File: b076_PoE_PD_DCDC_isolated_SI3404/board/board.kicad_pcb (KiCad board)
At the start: 2 copper layers, 45 x 29 mm, 40 parts, among them J1 013_PoE_rectified, J2 003_power, U1 Si3404, U2 FOD817A3SD, U3 TLV431

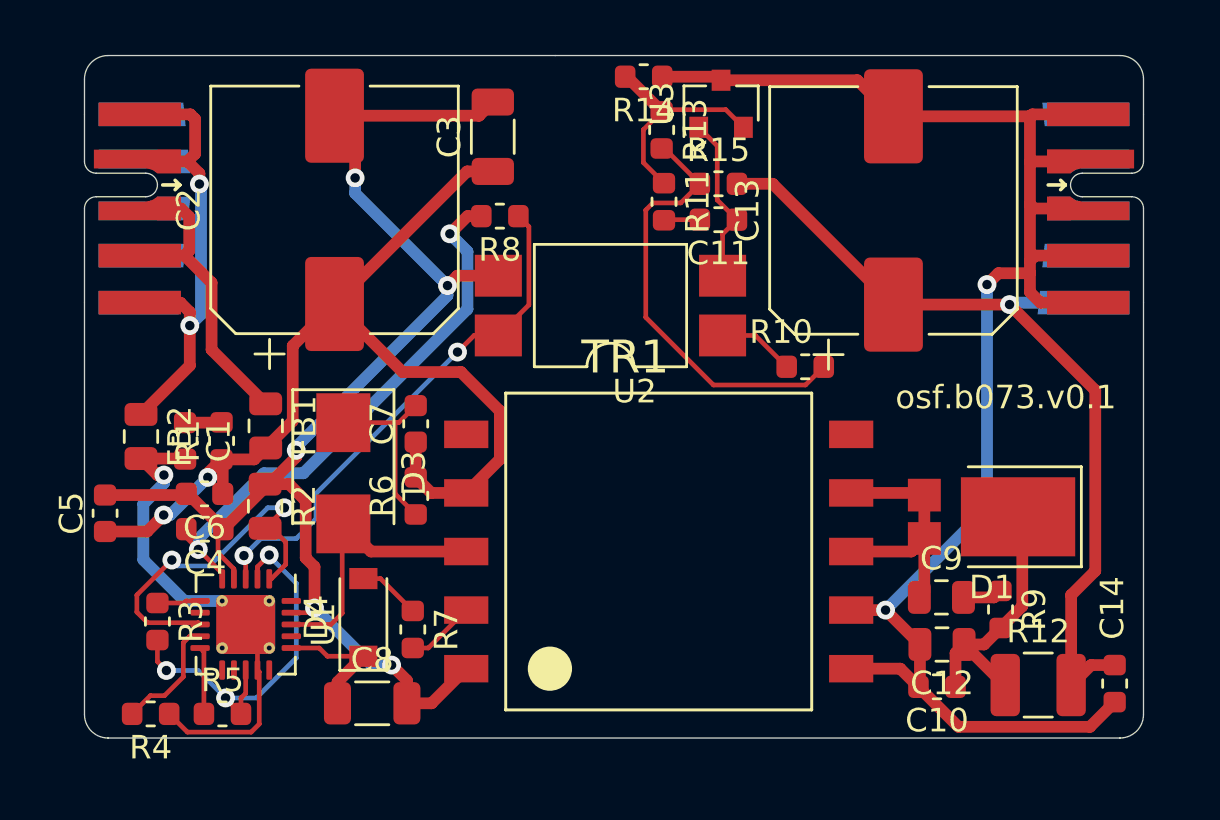
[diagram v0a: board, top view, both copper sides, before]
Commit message: cleaned up silkscreen
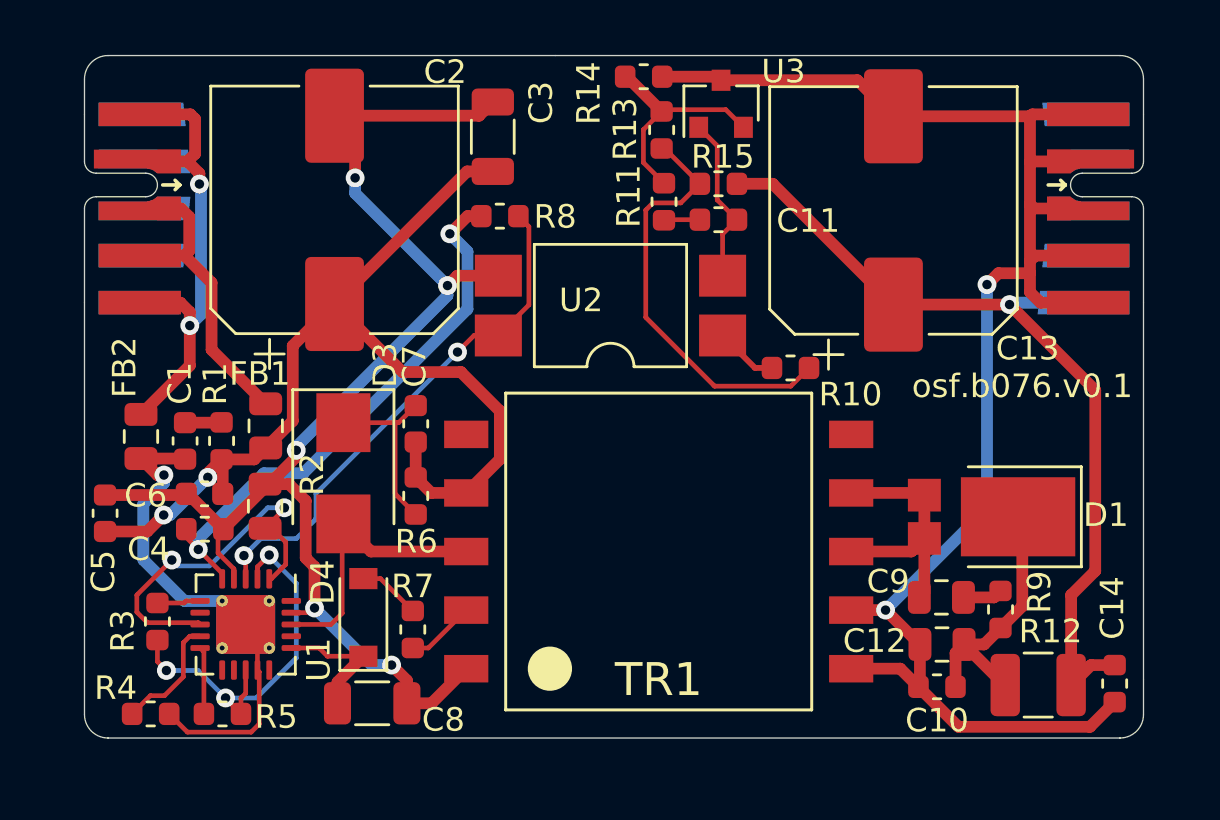
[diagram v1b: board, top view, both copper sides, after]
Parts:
- moved R10 0.63 mm to (160.0, 97.3)
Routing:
- net Net-(R10-Pad2): track 18.6 -> 18.0 mm
- net Net-(R10-Pad1): track 3.27 -> 2.67 mm
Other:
- board text added: "osf.b076.v0.1"
- board text removed: "osf.b073.v0.1"

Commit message: Update Symbol and relayout b076 dcdc
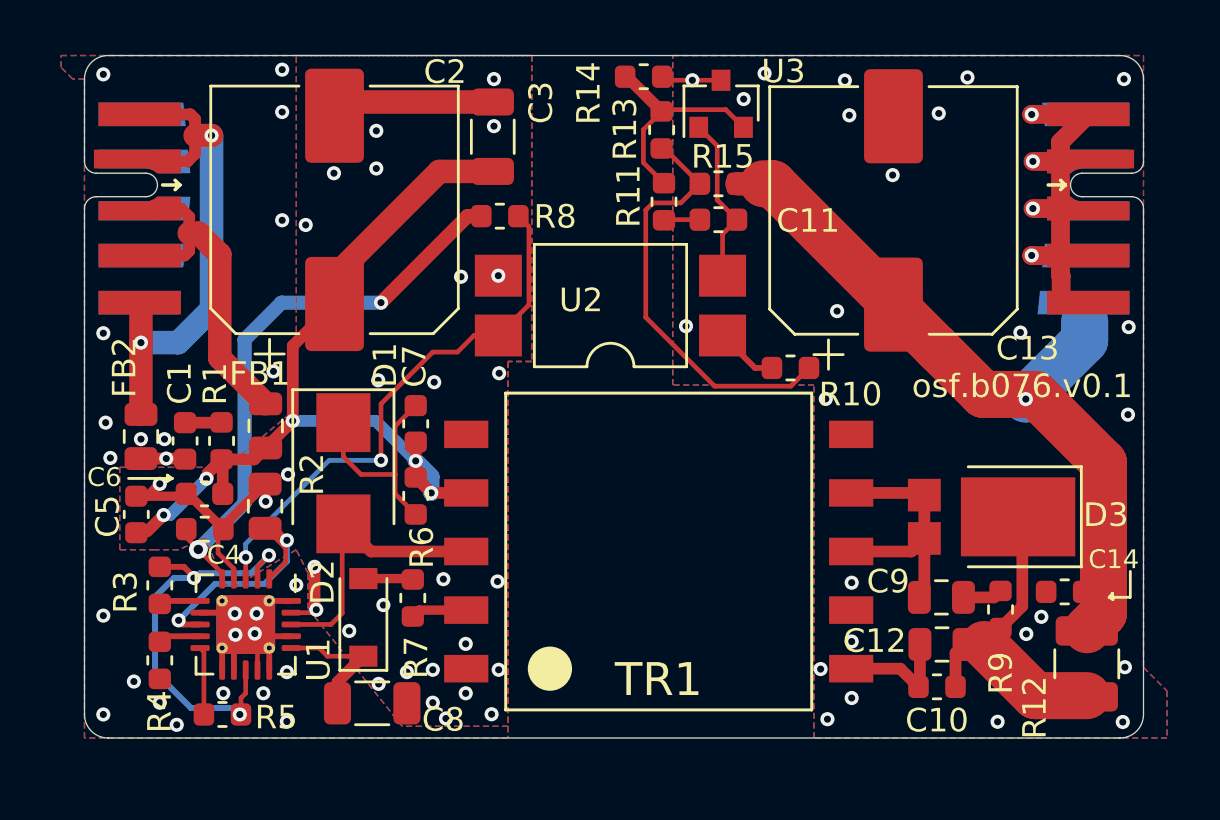
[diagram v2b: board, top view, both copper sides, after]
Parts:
- D3: renamed from D1; value SDT10A45P5 -> SDT10A45P5-13D
- TR1: value 749119950 -> TRANSF6
- U2: value FOD817A3SD -> LTV-827
- moved C14 4.44 mm to (171.7, 106.8), turned to 180 degrees
- moved R4 2.31 mm to (133.2, 109.7), turned to 90 degrees
- moved R12 2.25 mm to (172.6, 109.8), turned to 90 degrees
- moved R3 1.54 mm to (133.2, 106.5), turned to 90 degrees
- moved R7 1.34 mm to (143.9, 107.0)
- moved C5 1.33 mm to (132.2, 103.5)
- renumbered D3 to D1, D4 to D2
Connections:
- net Net-(C2-Pad1) renamed /dcdc/48V_IN
- C1 pad 2: Net-(C1-Pad2) -> /dcdc/GND_IN
- FB2 pad 2: Net-(C1-Pad2) -> /dcdc/GND_IN
- R4 pad 1: Net-(C1-Pad2) -> /dcdc/GND_IN
- U1 pad 11: unconnected-(U1-Pad11) -> /dcdc/GND_IN
- U1 pad 12: unconnected-(U1-Pad12) -> /dcdc/GND_IN
- U1 pad 14: Net-(C1-Pad2) -> /dcdc/GND_IN
- U1 pad 15: unconnected-(U1-Pad15) -> /dcdc/GND_IN
- U1 pad 17: unconnected-(U1-Pad17) -> /dcdc/GND_IN
- U1 pad 20: unconnected-(U1-Pad20) -> /dcdc/GND_IN
- U1 pad 21: Net-(C1-Pad2) -> /dcdc/GND_IN
- U1 pad 7: unconnected-(U1-Pad7) -> /dcdc/GND_IN
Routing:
- net /dcdc/GND2: track 69.7 -> 23.0 mm, vias 2 -> 29
- net VSS: track 58.2 -> 20.8 mm, vias 5 -> 29
- net Net-(C1-Pad2): track 19.9 -> 0.00 mm, vias 1 -> 0
- net /dcdc/GND_IN: track 0.00 -> 14.0 mm, vias 0 -> 25
- net /dcdc/48V_IN: track 43.2 -> 36.6 mm, vias 2 -> 5
- net Net-(R2-Pad2): track 15.8 -> 11.5 mm
- net /dcdc/5V: track 37.2 -> 33.0 mm
- net Net-(R4-Pad2): track 5.10 -> 1.81 mm
- net Net-(C10-Pad1): track 11.4 -> 14.2 mm
- net Net-(C7-Pad2): track 7.64 -> 9.31 mm
- net GND: track 20.1 -> 21.6 mm
- net /dcdc/48V: track 12.4 -> 13.5 mm
- net /dcdc/erout: track 22.1 -> 23.1 mm
- net VDD: track 23.8 -> 24.7 mm
- net Net-(R3-Pad2): track 17.1 -> 18.0 mm
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- added copper zone on B.Cu, net /dcdc/GND2
- added copper zone on F.Cu, net /dcdc/GND2
- added copper zone on B.Cu, net /dcdc/GND_IN
- added copper zone on F.Cu, net /dcdc/GND_IN
- added copper zone on B.Cu, net VSS
- added copper zone on F.Cu, net VSS

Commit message: Update edge connectors
reroute a little bit
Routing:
- net /dcdc/GND2: track 23.0 -> 26.6 mm, vias 29 -> 28
- net /dcdc/5V: track 33.0 -> 35.6 mm, vias 1 -> 3
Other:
- board text added: "osf.b076.v0.2"
- board text removed: "osf.b076.v0.1"
